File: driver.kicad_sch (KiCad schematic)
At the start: 83 parts, among them J2 BUTTERFLY, J4 SELECTOR, J5 SELECTOR_2, Q1 RJK0355DSP, Q2 RJK0355DSP, Q3 SiRC18DP, Q4 SiRC18DP, Q5 SiRC18DP, Q6 SiRC18DP, U2 LT3743, U3 MAX1978, U4 INA333xxDGK

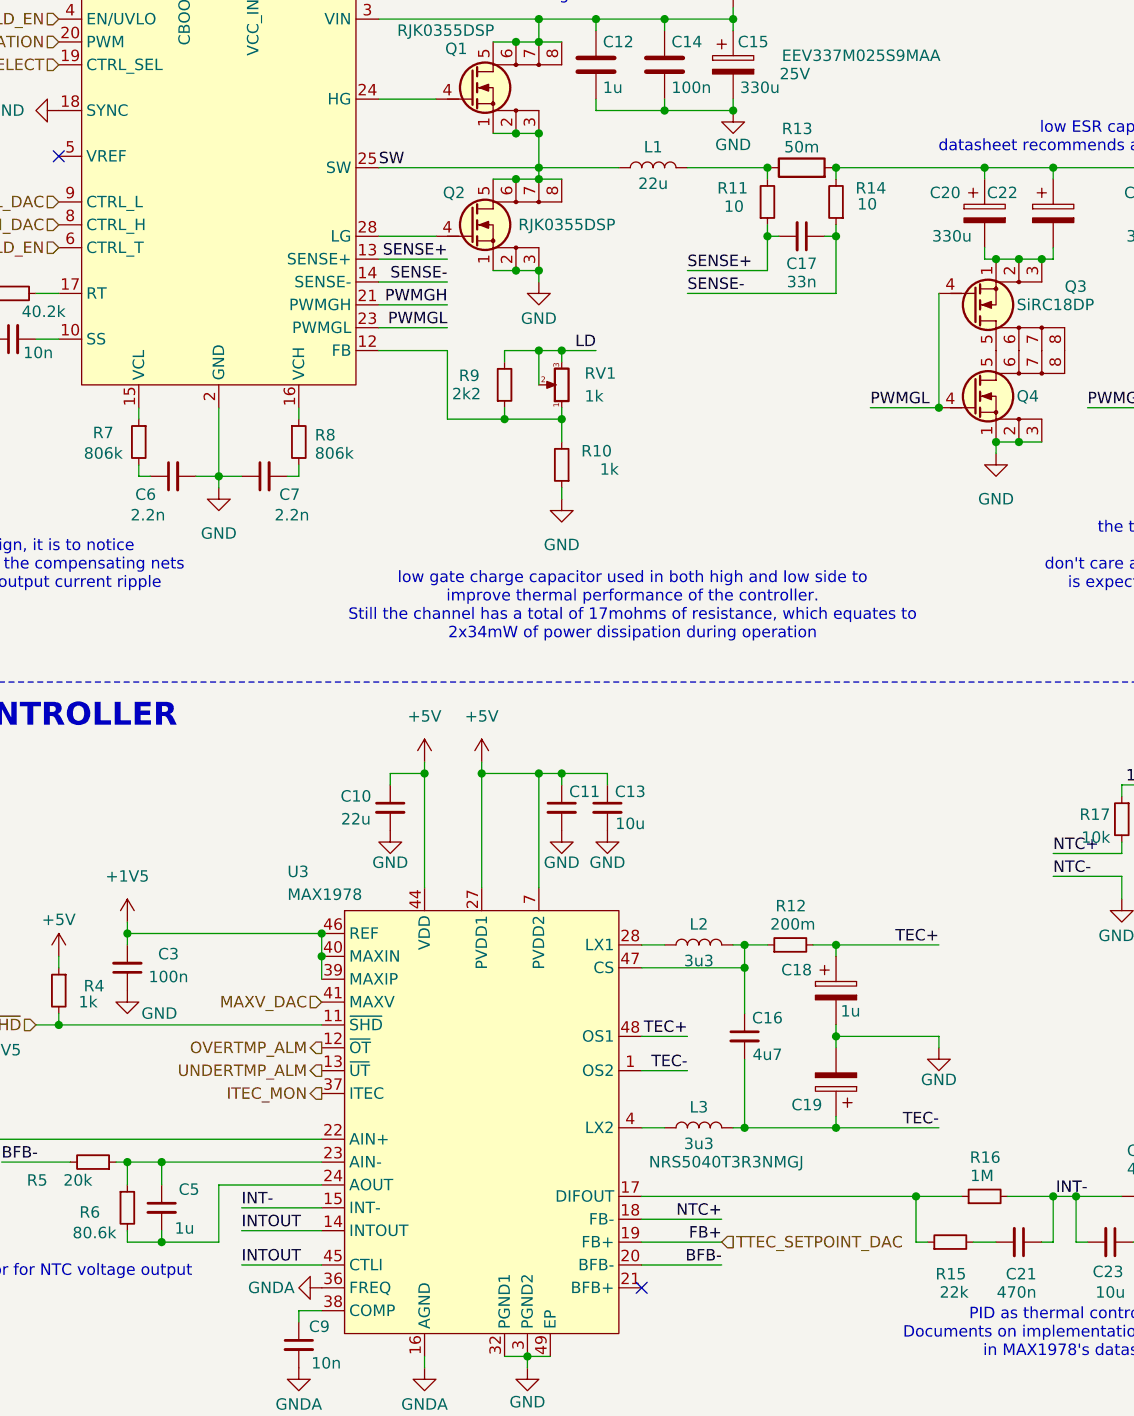
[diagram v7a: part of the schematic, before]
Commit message: fix: shorted PVDD and VDD on MIC
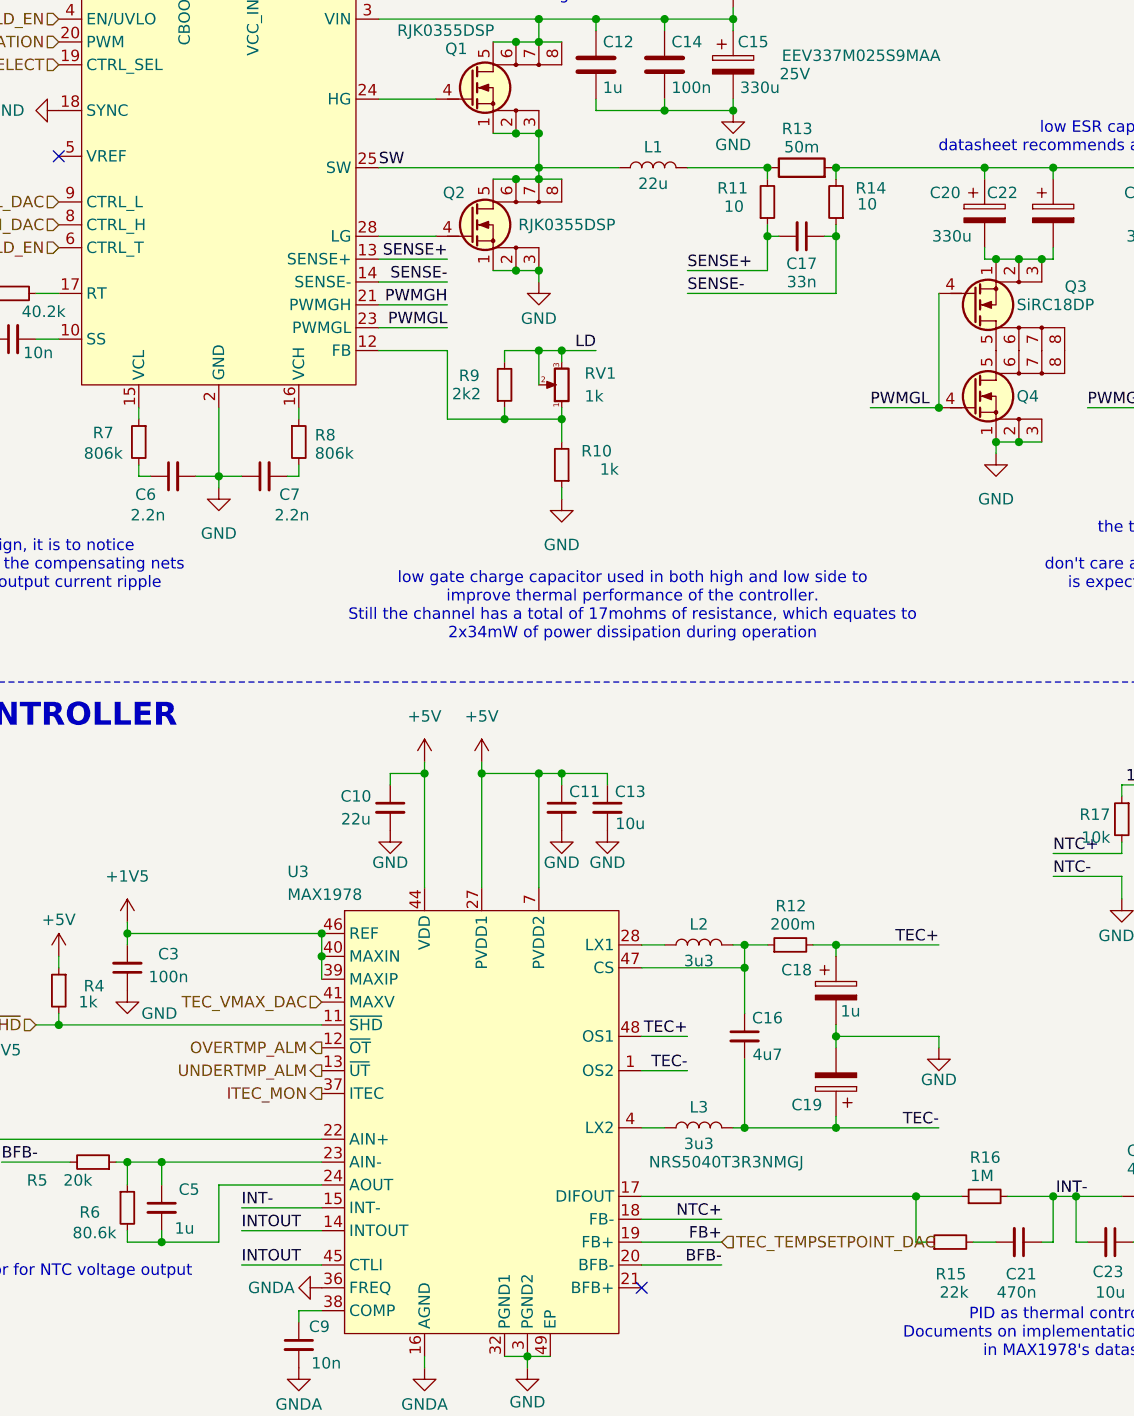
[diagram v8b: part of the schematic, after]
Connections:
- net MAXV_DAC: no longer U3.41 (MAXV)
- net TTEC_SETPOINT_DAC: no longer U3.19 (FB+)
- new net TEC_TEMPSETPOINT_DAC: U3.19 (FB+)
- new net TEC_VMAX_DAC: U3.41 (MAXV)
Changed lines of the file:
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@@
 (kicad_sch
-	(version 20231120)
+	(version 20241004)
 	(generator "eeschema")
-	(generator_version "8.0")
+	(generator_version "8.99")
 	(paper "A4")
 	(title_block
@@
 		(comment 1 "Mirco Tollardo")
 	)
+	(text "low gate charge capacitor used in both high and low side to \nimprove thermal performance of the controller.\nStill the channel has a total of 17mohms of resistance, which equates to \n2x34mW of power dissipation during operation"
+		(exclude_from_sim no)
+		(at 98.044 103.378 0)
+		(effects
+			(font
+				(size 1.27 1.27)
+			)
+		)
+	)
+	(text "low ESR caps should be used\ndatasheet recommends at least 50uF/A of load current"
+		(exclude_from_sim no)
+		(at 155.956 51.308 0)
+		(effects
+			(font
+				(size 1.27 1.27)
+			)
+		)
+	)
+	(text "Integrator for NTC voltage output"
+		(exclude_from_sim no)
+		(at 34.544 177.292 0)
+		(effects
+			(font
+				(size 1.27 1.27)
+			)
+		)
+	)
+	(text "TESTPOINTS"
+		(exclude_from_sim no)
+		(at 232.41 115.316 0)
+		(effects
+			(font
+				(size 2.54 2.54)
+				(thickness 0.508)
+				(bold yes)
+			)
+			(justify left)
+		)
+	)
+	(text "multiple parallel capacitors to lower total ESR"
+		(exclude_from_sim no)
+		(at 182.372 45.974 0)
+		(effects
+			(font
+				(size 1.27 1.27)
+			)
+		)
+	)
+	(text "modulation will be done by the fpga by changing the reference voltages\non CTRL_L and CTRL_H. CP/CC modes can be selected by the fpga"
+		(exclude_from_sim no)
+		(at 106.426 17.526 0)
+		(effects
+			(font
+				(size 1.27 1.27)
+			)
+		)
+	)
+	(text "Input caps as close as possible \nto the high side switch"
+		(exclude_from_sim no)
+		(at 92.456 34.544 0)
+		(effects
+			(font
+				(size 1.27 1.27)
+			)
+		)
+	)
+	(text "PID as thermal control loop.\nDocuments on implementation can be found \nin MAX1978's datasheet"
+		(exclude_from_sim no)
+		(at 147.574 184.15 0)
+		(effects
+			(font
+				(size 1.27 1.27)
+			)
+		)
+	)
+	(text "LASER DRIVER"
+		(exclude_from_sim no)
+		(at 26.67 16.002 0)
+		(effects
+			(font
+				(size 2.54 2.54)
+				(thickness 0.508)
+				(bold yes)
+			)
+		)
+	)
+	(text "By simulating the design, it is to notice \nthat incorrect dimensions of the compensating nets\ncan negatively influence output current ripple"
+		(exclude_from_sim no)
+		(at 25.654 98.806 0)
+		(effects
+			(font
+				(size 1.27 1.27)
+			)
+		)
+	)
+	(text "the transistors for capacitor switching should\nhave low channel resistance.\ndon't care about gate charges since modulation frequency \nis expected by requirements to reach 50kHz at most"
+		(exclude_from_sim no)
+		(at 169.418 97.79 0)
+		(effects
+			(font
+				(size 1.27 1.27)
+			)
+		)
+	)
+	(text "Gain = 1 + (100000/Rg)"
+		(exclude_from_sim no)
+		(at 263.398 93.472 0)
+		(effects
+			(font
+				(size 1.27 1.27)
+			)
+		)
+	)
+	(text "ADC POWER FILTERING"
+		(exclude_from_sim no)
+		(at 199.644 115.57 0)
+		(effects
+			(font
+				(size 2.54 2.54)
+				(thickness 0.508)
+				(bold yes)
+			)
+		)
+	)
+	(text "\n"
+		(exclude_from_sim no)
+		(at 204.724 171.704 0)
+		(effects
+			(font
+				(size 1.27 1.27)
+			)
+			(justify left)
+		)
+	)
+	(text "BUTTERFLY SOCKET"
+		(exclude_from_sim no)
+		(at 227.838 15.24 0)
+		(effects
+			(font
+				(size 2.54 2.54)
+				(thickness 0.508)
+				(bold yes)
+			)
+		)
+	)
+	(text "TEC CONTROLLER"
+		(exclude_from_sim no)
+		(at 30.226 115.57 0)
+		(effects
+			(font
+				(size 2.54 2.54)
+				(thickness 0.508)
+				(bold yes)
+			)
+		)
+	)
+	(text "CURRENT MONITOR"
+		(exclude_from_sim no)
+		(at 227.584 63.246 0)
+		(effects
+			(font
+				(size 2.54 2.54)
+				(thickness 0.508)
+				(bold yes)
+			)
+		)
+	)
 	(junction
 		(at 185.42 64.77)
@@
 		)
 	)
-	(text "low gate charge capacitor used in both high and low side to \nimprove thermal performance of the controller.\nStill the channel has a total of 17mohms of resistance, which equates to \n2x34mW of power dissipation during operation"
-		(exclude_from_sim no)
-		(at 98.044 103.378 0)
-		(effects
-			(font
-				(size 1.27 1.27)
-			)
-		)
-	)
-	(text "low ESR caps should be used\ndatasheet recommends at least 50uF/A of load current"
-		(exclude_from_sim no)
-		(at 155.956 51.308 0)
-		(effects
-			(font
-				(size 1.27 1.27)
-			)
-		)
-	)
-	(text "Integrator for NTC voltage output"
-		(exclude_from_sim no)
-		(at 34.544 177.292 0)
-		(effects
-			(font
-				(size 1.27 1.27)
-			)
-		)
-	)
-	(text "TESTPOINTS"
-		(exclude_from_sim no)
-		(at 232.41 115.316 0)
-		(effects
-			(font
-				(size 2.54 2.54)
-				(thickness 0.508)
-				(bold yes)
-			)
-			(justify left)
-		)
-	)
-	(text "multiple parallel capacitors to lower total ESR"
-		(exclude_from_sim no)
-		(at 182.372 45.974 0)
-		(effects
-			(font
-				(size 1.27 1.27)
-			)
-		)
-	)
-	(text "modulation will be done by the fpga by changing the reference voltages\non CTRL_L and CTRL_H. CP/CC modes can be selected by the fpga"
-		(exclude_from_sim no)
-		(at 106.426 17.526 0)
-		(effects
-			(font
-				(size 1.27 1.27)
-			)
-		)
-	)
-	(text "Input caps as close as possible \nto the high side switch"
-		(exclude_from_sim no)
-		(at 92.456 34.544 0)
-		(effects
-			(font
-				(size 1.27 1.27)
-			)
-		)
-	)
-	(text "PID as thermal control loop.\nDocuments on implementation can be found \nin MAX1978's datasheet"
-		(exclude_from_sim no)
-		(at 147.574 184.15 0)
-		(effects
-			(font
-				(size 1.27 1.27)
-			)
-		)
-	)
-	(text "LASER DRIVER"
-		(exclude_from_sim no)
-		(at 26.67 16.002 0)
-		(effects
-			(font
-				(size 2.54 2.54)
-				(thickness 0.508)
-				(bold yes)
-			)
-		)
-	)
-	(text "By simulating the design, it is to notice \nthat incorrect dimensions of the compensating nets\ncan negatively influence output current ripple"
-		(exclude_from_sim no)
-		(at 25.654 98.806 0)
-		(effects
-			(font
-				(size 1.27 1.27)
-			)
-		)
-	)
-	(text "the transistors for capacitor switching should\nhave low channel resistance.\ndon't care about gate charges since modulation frequency \nis expected by requirements to reach 50kHz at most"
-		(exclude_from_sim no)
-		(at 169.418 97.79 0)
-		(effects
-			(font
-				(size 1.27 1.27)
-			)
-		)
-	)
-	(text "Gain = 1 + (100000/Rg)"
-		(exclude_from_sim no)
-		(at 263.398 93.472 0)
-		(effects
-			(font
-				(size 1.27 1.27)
-			)
-		)
-	)
-	(text "ADC POWER FILTERING"
-		(exclude_from_sim no)
-		(at 199.644 115.57 0)
-		(effects
-			(font
-				(size 2.54 2.54)
-				(thickness 0.508)
-				(bold yes)
-			)
-		)
-	)
-	(text "\n"
-		(exclude_from_sim no)
-		(at 204.724 171.704 0)
-		(effects
-			(font
-				(size 1.27 1.27)
-			)
-			(justify left)
-		)
-	)
-	(text "BUTTERFLY SOCKET"
-		(exclude_from_sim no)
-		(at 227.838 15.24 0)
-		(effects
-			(font
-				(size 2.54 2.54)
-				(thickness 0.508)
-				(bold yes)
-			)
-		)
-	)
-	(text "TEC CONTROLLER"
-		(exclude_from_sim no)
-		(at 30.226 115.57 0)
-		(effects
-			(font
-				(size 2.54 2.54)
-				(thickness 0.508)
-				(bold yes)
-			)
-		)
-	)
-	(text "CURRENT MONITOR"
-		(exclude_from_sim no)
-		(at 227.584 63.246 0)
-		(effects
-			(font
-				(size 2.54 2.54)
-				(thickness 0.508)
-				(bold yes)
-			)
-		)
-	)
 	(label "1V5ADC"
 		(at 208.28 134.62 0)
@@
 		)
 	)
-	(hierarchical_label "TTEC_SETPOINT_DAC"
+	(hierarchical_label "TEC_TEMPSETPOINT_DAC"
 		(shape input)
 		(at 107.95 173.99 0)
@@
 		)
 	)
-	(hierarchical_label "MAXV_DAC"
+	(hierarchical_label "TEC_VMAX_DAC"
 		(shape input)
 		(at 63.5 147.32 180)
